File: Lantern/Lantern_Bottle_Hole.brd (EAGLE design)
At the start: 82 x 82 mm, 0 parts

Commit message: Fixed Resistors
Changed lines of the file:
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@@
 <setting verticaltext="up"/>
 </settings>
-<grid distance="50" unitdist="mil" unit="mil" style="lines" multiple="1" display="yes" altdistance="5" altunitdist="mil" altunit="mil"/>
+<grid distance="50" unitdist="mil" unit="mm" style="lines" multiple="1" display="yes" altdistance="5" altunitdist="mil" altunit="mil"/>
 <layers>
 <layer number="1" name="Top" color="4" fill="1" visible="yes" active="yes"/>
@@
 </layers>
 <board>
-<fusionsync huburn="a.YnVzaW5lc3M6YWlwaWxvdA" projecturn="a.YnVzaW5lc3M6YWlwaWxvdCMyMDIxMDEwNTM2ODY3ODk4MQ" f3durn="urn:adsk.wipprod:dm.lineage:U1T2WxYnQzGHzBcJk5poig" pcbguid="" lastpulledtime="" lastsyncedchangeguid="" latestrevisionid="4c40cfeb-6b9e-4e3f-b84f-d7fd449d8e40" lastsyncedrevisionid="4c40cfeb-6b9e-4e3f-b84f-d7fd449d8e40" lastboardhashguid="5ad489bf-aa54-e20f-2331-04c2f75d86ee" lastpushedtime="2021-01-07T19:34:20Z" linktopcb3d="true"/>
+<fusionsync huburn="a.YnVzaW5lc3M6YWlwaWxvdA" projecturn="a.YnVzaW5lc3M6YWlwaWxvdCMyMDIxMDEwNTM2ODY3ODk4MQ" f3durn="urn:adsk.wipprod:dm.lineage:U1T2WxYnQzGHzBcJk5poig" pcbguid="" lastpulledtime="" lastsyncedchangeguid="" latestrevisionid="1a5ce7b9-13bd-4726-829e-83396a1b6eea" lastsyncedrevisionid="1a5ce7b9-13bd-4726-829e-83396a1b6eea" lastboardhashguid="fd884b8e-4090-9bb7-e282-c3081c861e12" lastpushedtime="2021-01-15T14:01:54Z" linktopcb3d="true"/>
 <plain>
 <hole x="0" y="0" drill="61"/>
@@
 <signals>
 <signal name="S$1">
-<via x="-31.2" y="-18" extent="1-16" drill="4.3"/>
+<via x="-31.2" y="-18" extent="1-16" drill="4.3" diameter="7.9"/>
 </signal>
 <signal name="S$2">
-<via x="31.2" y="-18" extent="1-16" drill="4.3"/>
+<via x="31.2" y="-18" extent="1-16" drill="4.3" diameter="7.9"/>
 </signal>
 <signal name="GND">
@@
 <vertex x="-41.91" y="41.91"/>
 </polygon>
-<via x="-35.75" y="0" extent="1-16" drill="4.3"/>
-<via x="0" y="35.75" extent="1-16" drill="4.3"/>
-<via x="35.75" y="0" extent="1-16" drill="4.3"/>
+<via x="-35.75" y="0" extent="1-16" drill="4.3" diameter="7.9"/>
+<via x="0" y="35.75" extent="1-16" drill="4.3" diameter="7.9"/>
+<via x="35.75" y="0" extent="1-16" drill="4.3" diameter="7.9"/>
 </signal>
 </signals>

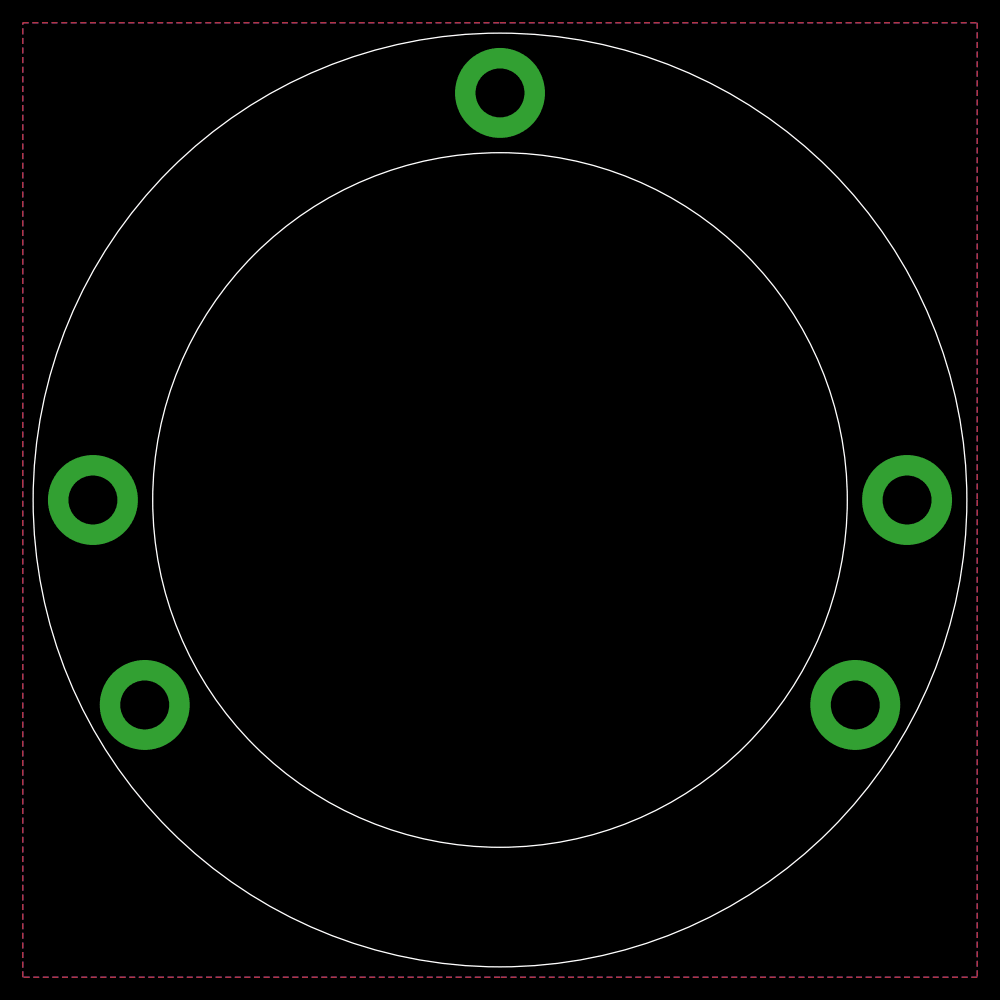
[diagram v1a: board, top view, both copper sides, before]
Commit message: DRC fix
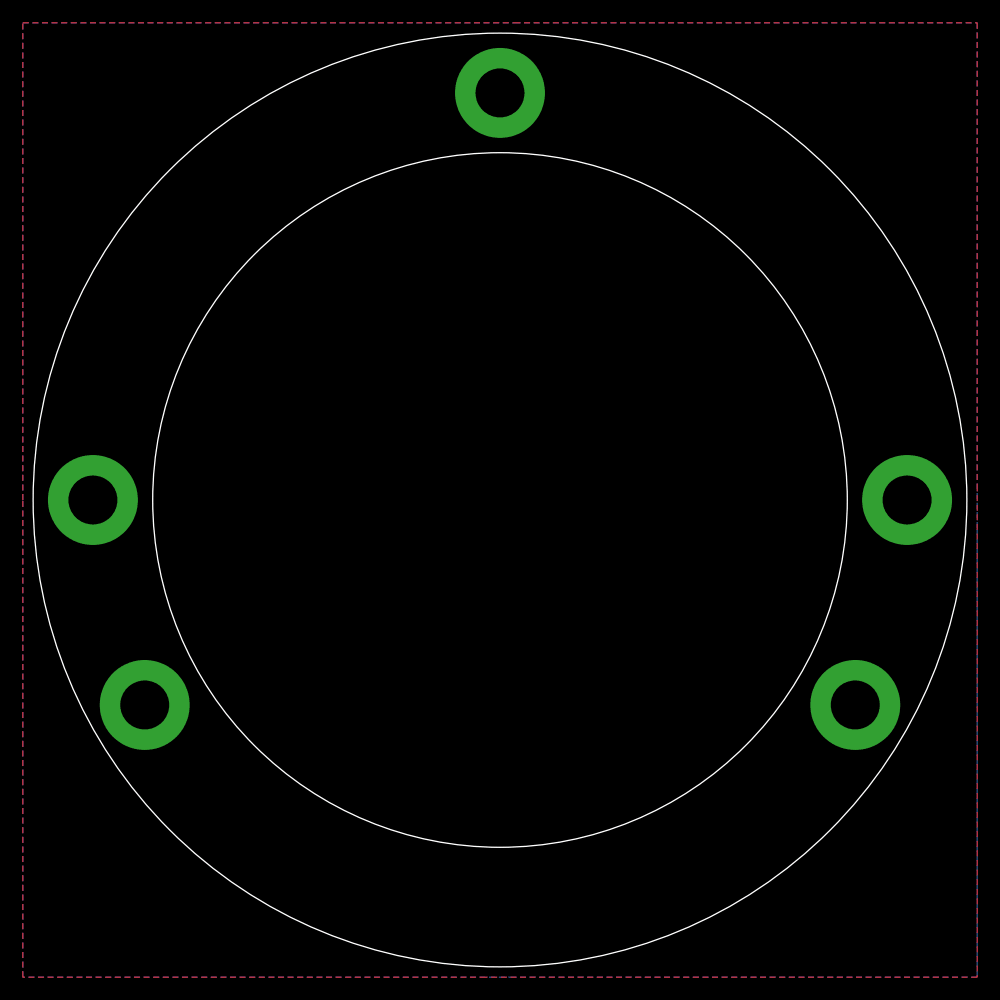
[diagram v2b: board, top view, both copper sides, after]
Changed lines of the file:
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@@
 <setting verticaltext="up"/>
 </settings>
-<grid distance="50" unitdist="mil" unit="mm" style="lines" multiple="1" display="yes" altdistance="5" altunitdist="mil" altunit="mil"/>
+<grid distance="50" unitdist="mil" unit="mil" style="lines" multiple="1" display="yes" altdistance="5" altunitdist="mil" altunit="mil"/>
 <layers>
 <layer number="1" name="Top" color="4" fill="1" visible="yes" active="yes"/>
@@
 </layers>
 <board>
-<fusionsync huburn="a.YnVzaW5lc3M6YWlwaWxvdA" projecturn="a.YnVzaW5lc3M6YWlwaWxvdCMyMDIxMDEwNTM2ODY3ODk4MQ" f3durn="urn:adsk.wipprod:dm.lineage:U1T2WxYnQzGHzBcJk5poig" pcbguid="" lastpulledtime="" lastsyncedchangeguid="" latestrevisionid="1a5ce7b9-13bd-4726-829e-83396a1b6eea" lastsyncedrevisionid="1a5ce7b9-13bd-4726-829e-83396a1b6eea" lastboardhashguid="fd884b8e-4090-9bb7-e282-c3081c861e12" lastpushedtime="2021-01-15T14:01:54Z" linktopcb3d="true"/>
+<fusionsync huburn="a.YnVzaW5lc3M6YWlwaWxvdA" projecturn="a.YnVzaW5lc3M6YWlwaWxvdCMyMDIxMDEwNTM2ODY3ODk4MQ" f3durn="urn:adsk.wipprod:dm.lineage:U1T2WxYnQzGHzBcJk5poig" pcbguid="" lastpulledtime="" lastsyncedchangeguid="" latestrevisionid="f3508f9e-8fac-4160-af76-27ea6afecb7c" lastsyncedrevisionid="f3508f9e-8fac-4160-af76-27ea6afecb7c" lastboardhashguid="e412a0f0-6808-67ed-857b-dfeeb406f637" lastpushedtime="2021-01-15T22:14:21Z" linktopcb3d="true"/>
 <plain>
 <hole x="0" y="0" drill="61"/>
@@
 </class>
 </classes>
-<designrules name="default">
-<description language="de">&lt;b&gt;EAGLE Design Rules&lt;/b&gt;
+<designrules name="jlcpcb2layer *">
+<description language="en">&lt;b&gt;JLCPCB Design Rules by Jaap de Dood&lt;/b&gt;
 &lt;p&gt;
-Die Standard-Design-Rules sind so gewählt, dass sie für
-die meisten Anwendungen passen. Sollte ihre Platine
-besondere Anforderungen haben, treffen Sie die erforderlichen
-Einstellungen hier und speichern die Design Rules unter
-einem neuen Namen ab.</description>
-<description language="en">&lt;b&gt;EAGLE Design Rules&lt;/b&gt;
-&lt;p&gt;
-The default Design Rules have been set to cover
-a wide range of applications. Your particular design
-may have different requirements, so please make the
-necessary adjustments and save your customized
-design rules under a new name.</description>
+Please make sure your boards conform to these design rules.
+&lt;/p&gt;</description>
 <param name="layerSetup" value="(1*16)"/>
-<param name="mtCopper" value="0.035mm 0.035mm 0.035mm 0.035mm 0.035mm 0.035mm 0.035mm 0.035mm 0.035mm 0.035mm 0.035mm 0.035mm 0.035mm 0.035mm 0.035mm 0.035mm"/>
-<param name="mtIsolate" value="1.5mm 0.15mm 0.2mm 0.15mm 0.2mm 0.15mm 0.2mm 0.15mm 0.2mm 0.15mm 0.2mm 0.15mm 0.2mm 0.15mm 0.2mm"/>
-<param name="mdWireWire" value="6mil"/>
-<param name="mdWirePad" value="6mil"/>
-<param name="mdWireVia" value="6mil"/>
-<param name="mdPadPad" value="6mil"/>
-<param name="mdPadVia" value="6mil"/>
-<param name="mdViaVia" value="6mil"/>
-<param name="mdSmdPad" value="6mil"/>
-<param name="mdSmdVia" value="6mil"/>
-<param name="mdSmdSmd" value="6mil"/>
-<param name="mdViaViaSameLayer" value="6mil"/>
+<param name="mtCopper" value="0.035559375mm 0.0356mm 0.0356mm 0.0356mm 0.0356mm 0.0356mm 0.0356mm 0.0356mm 0.0356mm 0.0356mm 0.0356mm 0.0356mm 0.0356mm 0.0356mm 0.0356mm 0.035559375mm"/>
+<param name="mtIsolate" value="1.6mm 0.1499mm 0.2007mm 0.1499mm 0.2007mm 0.1499mm 0.2007mm 0.1499mm 0.2007mm 0.1499mm 0.2007mm 0.1499mm 0.2007mm 0.1499mm 0.2007mm"/>
+<param name="mdWireWire" value="5mil"/>
+<param name="mdWirePad" value="5mil"/>
+<param name="mdWireVia" value="20mil"/>
+<param name="mdPadPad" value="5mil"/>
+<param name="mdPadVia" value="5mil"/>
+<param name="mdViaVia" value="5mil"/>
+<param name="mdSmdPad" value="5mil"/>
+<param name="mdSmdVia" value="5mil"/>
+<param name="mdSmdSmd" value="5mil"/>
+<param name="mdViaViaSameLayer" value="8mil"/>
 <param name="mnLayersViaInSmd" value="2"/>
-<param name="mdCopperDimension" value="40mil"/>
+<param name="mdCopperDimension" value="8mil"/>
 <param name="mdDrill" value="6mil"/>
 <param name="mdSmdStop" value="0mil"/>
-<param name="msWidth" value="6mil"/>
-<param name="msDrill" value="0.35mm"/>
-<param name="msMicroVia" value="9.99mm"/>
+<param name="msWidth" value="5mil"/>
+<param name="msDrill" value="12mil"/>
+<param name="msMicroVia" value="12mil"/>
 <param name="msBlindViaRatio" value="0.5"/>
 <param name="rvPadTop" value="0.25"/>
@@
 <param name="rvMicroViaOuter" value="0.25"/>
 <param name="rvMicroViaInner" value="0.25"/>
-<param name="rlMinPadTop" value="10mil"/>
+<param name="rlMinPadTop" value="5mil"/>
 <param name="rlMaxPadTop" value="20mil"/>
-<param name="rlMinPadInner" value="10mil"/>
+<param name="rlMinPadInner" value="5mil"/>
 <param name="rlMaxPadInner" value="20mil"/>
-<param name="rlMinPadBottom" value="10mil"/>
+<param name="rlMinPadBottom" value="5mil"/>
 <param name="rlMaxPadBottom" value="20mil"/>
-<param name="rlMinViaOuter" value="8mil"/>
+<param name="rlMinViaOuter" value="3mil"/>
 <param name="rlMaxViaOuter" value="20mil"/>
-<param name="rlMinViaInner" value="8mil"/>
+<param name="rlMinViaInner" value="3mil"/>
 <param name="rlMaxViaInner" value="20mil"/>
-<param name="rlMinMicroViaOuter" value="4mil"/>
+<param name="rlMinMicroViaOuter" value="3mil"/>
 <param name="rlMaxMicroViaOuter" value="20mil"/>
-<param name="rlMinMicroViaInner" value="4mil"/>
+<param name="rlMinMicroViaInner" value="3mil"/>
 <param name="rlMaxMicroViaInner" value="20mil"/>
 <param name="psTop" value="-1"/>
@@
 <param name="mvStopFrame" value="1"/>
 <param name="mvCreamFrame" value="0"/>
-<param name="mlMinStopFrame" value="4mil"/>
-<param name="mlMaxStopFrame" value="4mil"/>
+<param name="mlMinStopFrame" value="2.5mil"/>
+<param name="mlMaxStopFrame" value="2.5mil"/>
 <param name="mlMinCreamFrame" value="0mil"/>
 <param name="mlMaxCreamFrame" value="0mil"/>
@@
 </elements>
 <signals>
-<signal name="S$1">
+<signal name="NC">
+<via x="-35.75" y="0" extent="1-16" drill="4.3" diameter="7.9"/>
+<via x="0" y="35.75" extent="1-16" drill="4.3" diameter="7.9"/>
+<via x="35.75" y="0" extent="1-16" drill="4.3" diameter="7.9"/>
 <via x="-31.2" y="-18" extent="1-16" drill="4.3" diameter="7.9"/>
-</signal>
-<signal name="S$2">
 <via x="31.2" y="-18" extent="1-16" drill="4.3" diameter="7.9"/>
+<wire x1="-35.75" y1="0" x2="-31.2" y2="-18" width="0" layer="19" extent="1-1"/>
+<wire x1="0" y1="35.75" x2="-35.75" y2="0" width="0" layer="19" extent="1-1"/>
+<wire x1="35.75" y1="0" x2="0" y2="35.75" width="0" layer="19" extent="1-1"/>
+<wire x1="31.2" y1="-18" x2="35.75" y2="0" width="0" layer="19" extent="1-1"/>
 </signal>
 <signal name="GND">
 <polygon width="0.1524" layer="1">
-<vertex x="0" y="41.91"/>
+<vertex x="-41.91" y="0"/>
+<vertex x="-41.91" y="41.91"/>
+<vertex x="1.27" y="41.91"/>
 <vertex x="41.91" y="41.91"/>
-<vertex x="41.91" y="0"/>
+<vertex x="41.91" y="1.27"/>
 <vertex x="41.91" y="-41.91"/>
-<vertex x="0" y="-41.91"/>
+<vertex x="-1.27" y="-41.91"/>
 <vertex x="-41.91" y="-41.91"/>
-<vertex x="-41.91" y="1.27"/>
-<vertex x="-41.91" y="41.91"/>
 </polygon>
 <polygon width="0.1524" layer="16">
-<vertex x="0" y="41.91"/>
+<vertex x="-41.91" y="0"/>
+<vertex x="-41.91" y="41.91"/>
+<vertex x="1.27" y="41.91"/>
 <vertex x="41.91" y="41.91"/>
-<vertex x="41.91" y="0"/>
+<vertex x="41.91" y="-2.54"/>
 <vertex x="41.91" y="-41.91"/>
-<vertex x="0" y="-41.91"/>
+<vertex x="1.27" y="-41.91"/>
 <vertex x="-41.91" y="-41.91"/>
-<vertex x="-41.91" y="1.27"/>
-<vertex x="-41.91" y="41.91"/>
 </polygon>
-<via x="-35.75" y="0" extent="1-16" drill="4.3" diameter="7.9"/>
-<via x="0" y="35.75" extent="1-16" drill="4.3" diameter="7.9"/>
-<via x="35.75" y="0" extent="1-16" drill="4.3" diameter="7.9"/>
 </signal>
 </signals>
@@
 <mfgpreviewcolor name="substratecolor" color="0xFF786E46"/>
 </mfgpreviewcolors>
+<errors>
+</errors>
 </board>
 </drawing>
